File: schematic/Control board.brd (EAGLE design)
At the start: 41.6 x 67.3 mm, 14 parts, among them IC2 ATTINY44A

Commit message: Updated schematic, board file, and library; also updated the 3D model
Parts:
- moved POW1 3.86 mm to (24.1, 57.1)
- moved C1 3.86 mm to (19.1, 17.1), turned to 0 degrees
- moved REG1 3.86 mm to (20.3, 20.3)
- moved C2 3.24 mm to (26.7, 20.3), turned to 270 degrees
- renumbered ROTARY to ROTARY_P0915N, SLIDE to SLIDE_PTA2043
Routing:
- net +12V: track 89.6 -> 82.3 mm
- net +5V: track 100.6 -> 105.4 mm
- net GND: track 20.7 -> 16.1 mm
- net N$4: track 14.3 -> 13.4 mm

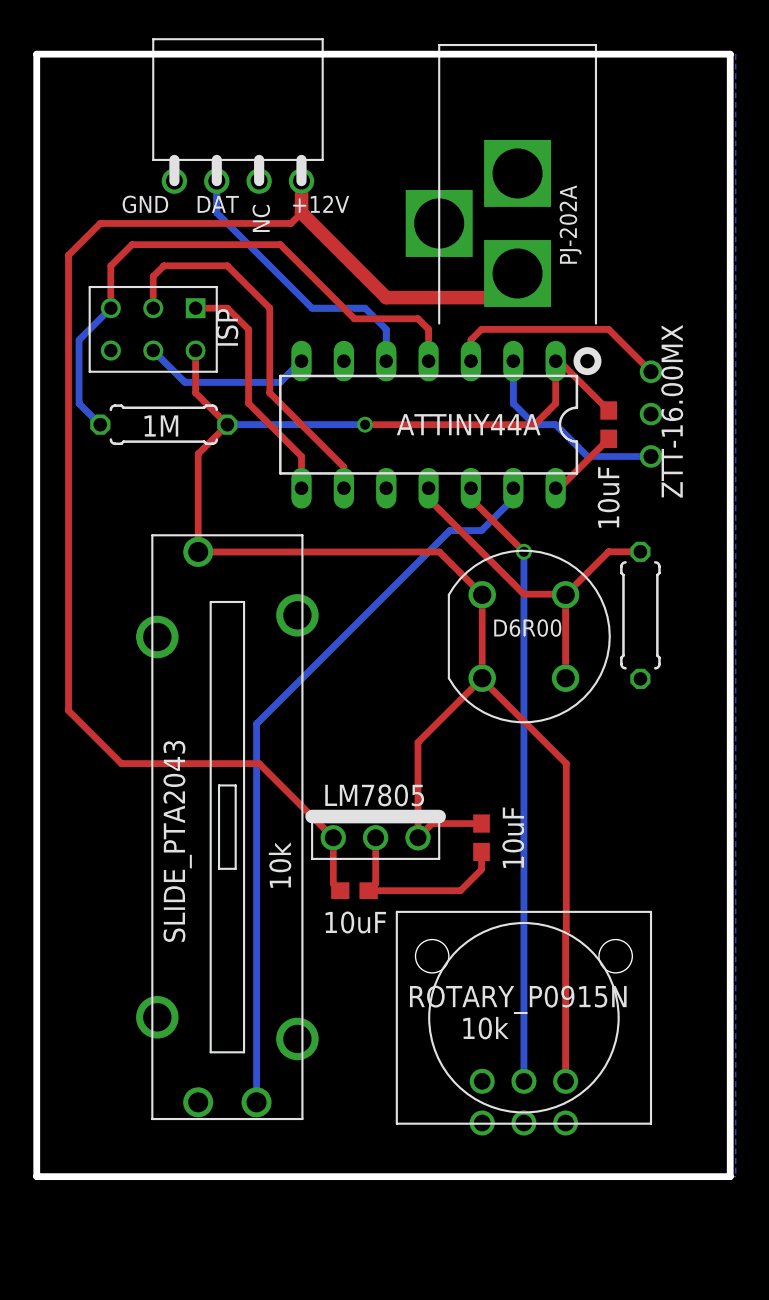
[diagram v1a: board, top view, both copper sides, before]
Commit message: Voltage regulator and DIP microcontroller are too big, replacing with small SMD components
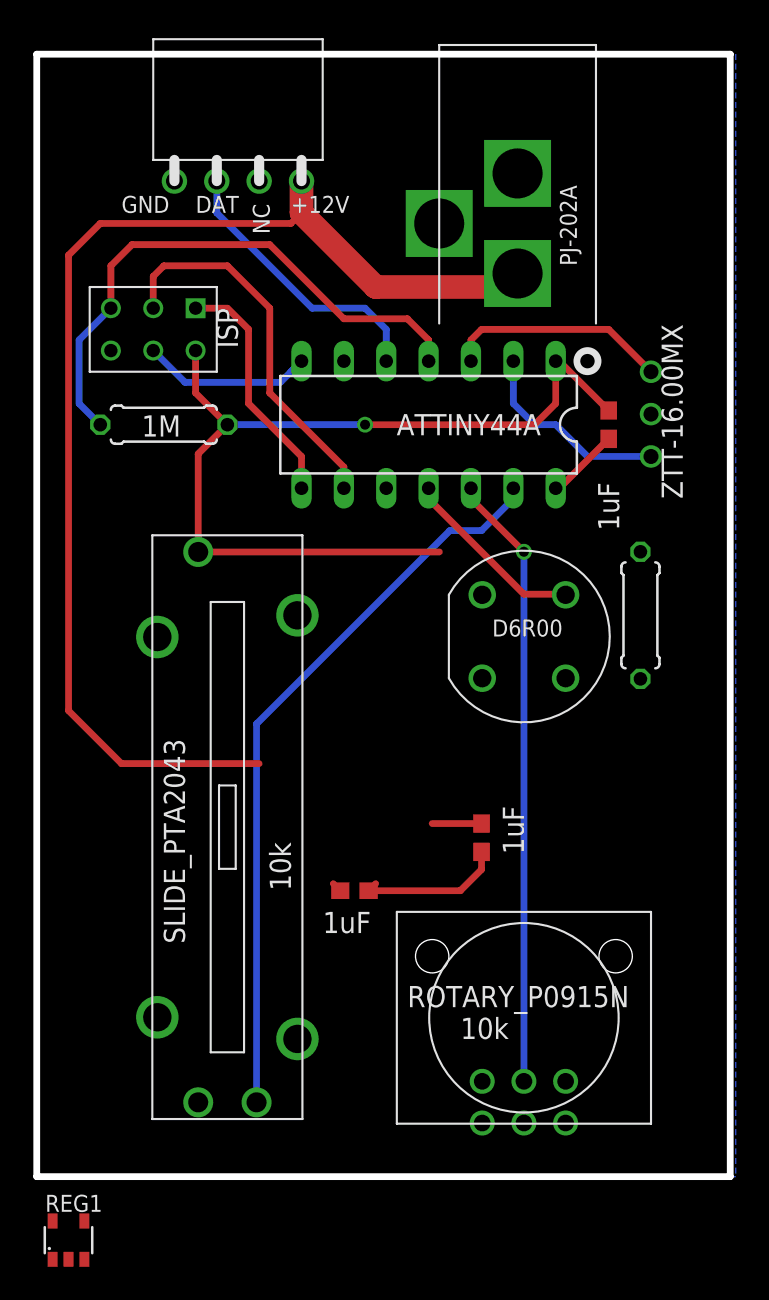
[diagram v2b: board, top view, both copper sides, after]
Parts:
- C1, C2, C3: value 10uF -> 1uF
- REG1: value LM7805 -> MIC5205; device RGB LED project:VREG_THROUGHHOLE -> RGB LED project:SOT-23-5
- moved REG1 30.4 mm to (1.91, -3.81)
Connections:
- net +12V: now also REG1.3
- net +5V: now also REG1.5; no longer REG1.3
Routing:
- net +5V: track 105.4 -> 58.2 mm
- net COLOR_SW: track 21.8 -> 11.2 mm
- net +12V: track 82.3 -> 72.7 mm
- net GND: track 16.1 -> 13.3 mm
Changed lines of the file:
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@@
 </autorouter>
 <elements>
-<element name="C1" library="resistor" package="C0603" value="10uF" x="19.05" y="17.145" smashed="yes">
+<element name="C1" library="resistor" package="C0603" value="1uF" x="19.05" y="17.145" smashed="yes">
 <attribute name="VALUE" x="17.145" y="14.605" size="1.27" layer="21" font="vector"/>
 </element>
@@
 </element>
 <element name="U$1" library="RGB LED project" package="ISP" value="ISP" x="6.985" y="50.8" smashed="yes" rot="R270"/>
-<element name="REG1" library="RGB LED project" package="VREG_THROUGHHOLE" value="LM7805" x="20.32" y="20.32" smashed="yes">
-<attribute name="VALUE" x="17.145" y="22.225" size="1.27" layer="21" font="vector"/>
-</element>
-<element name="C2" library="resistor" package="C0603" value="10uF" x="26.67" y="20.32" smashed="yes" rot="R270">
+<element name="C2" library="resistor" package="C0603" value="1uF" x="26.67" y="20.32" smashed="yes" rot="R270">
 <attribute name="VALUE" x="27.94" y="22.225" size="1.27" layer="21" font="vector" rot="R270"/>
 </element>
-<element name="C3" library="resistor" package="C0603" value="10uF" x="34.29" y="45.085" smashed="yes" rot="R270">
+<element name="C3" library="resistor" package="C0603" value="1uF" x="34.29" y="45.085" smashed="yes" rot="R270">
 <attribute name="VALUE" x="34.925" y="38.735" size="1.27" layer="21" font="vector" rot="R90"/>
 </element>
+<element name="REG1" library="RGB LED project" package="SOT-23-5" value="MIC5205" x="1.905" y="-3.81"/>
 </elements>
 <signals>
 <signal name="+5V">
 <contactref element="SLIDE_PTA2043" pad="P3"/>
-<contactref element="ROTARY_P0915N" pad="R13"/>
-<contactref element="S1" pad="1A"/>
-<contactref element="S1" pad="2A"/>
 <contactref element="IC2" pad="1"/>
 <contactref element="U$1" pad="VCC"/>
 <contactref element="R3" pad="1"/>
-<wire x1="26.71" y1="34.885" x2="26.71" y2="29.885" width="0.4064" layer="1"/>
-<contactref element="REG1" pad="3"/>
 <contactref element="C2" pad="1"/>
 <contactref element="C3" pad="1"/>
@@
 <wire x1="9.68" y1="43.335" x2="11.43" y2="45.085" width="0.4064" layer="1"/>
 <wire x1="9.68" y1="37.455" x2="24.14" y2="37.455" width="0.4064" layer="1"/>
-<wire x1="24.14" y1="37.455" x2="26.71" y2="34.885" width="0.4064" layer="1"/>
-<wire x1="31.71" y1="5.715" x2="31.71" y2="14.645" width="0.4064" layer="1"/>
-<wire x1="26.71" y1="29.885" x2="26.71" y2="29.805" width="0.4064" layer="1"/>
-<wire x1="26.71" y1="29.805" x2="31.75" y2="24.765" width="0.4064" layer="1"/>
-<wire x1="31.75" y1="24.765" x2="31.75" y2="14.685" width="0.4064" layer="1"/>
-<wire x1="31.75" y1="14.685" x2="31.71" y2="14.645" width="0.4064" layer="1"/>
 <wire x1="31.115" y1="48.895" x2="31.115" y2="46.355" width="0.4064" layer="1"/>
 <wire x1="31.115" y1="46.355" x2="29.845" y2="45.085" width="0.4064" layer="1"/>
@@
 <via x="19.685" y="45.085" extent="1-16" drill="0.6"/>
 <wire x1="19.685" y1="45.085" x2="11.43" y2="45.085" width="0.4064" layer="16"/>
-<wire x1="22.86" y1="20.32" x2="22.86" y2="26.035" width="0.4064" layer="1"/>
-<wire x1="22.86" y1="26.035" x2="26.71" y2="29.885" width="0.4064" layer="1"/>
 <wire x1="26.67" y1="21.17" x2="23.71" y2="21.17" width="0.4064" layer="1"/>
-<wire x1="23.71" y1="21.17" x2="22.86" y2="20.32" width="0.4064" layer="1"/>
+<contactref element="REG1" pad="5"/>
+<contactref element="S1" pad="1A"/>
+<contactref element="S1" pad="2A"/>
+<contactref element="ROTARY_P0915N" pad="R13"/>
+<wire x1="24.14" y1="37.455" x2="26.71" y2="34.885" width="0" layer="19" extent="1-1"/>
+<wire x1="26.71" y1="29.885" x2="26.71" y2="34.885" width="0" layer="19" extent="1-1"/>
+<wire x1="26.67" y1="21.17" x2="26.71" y2="29.885" width="0" layer="19" extent="1-1"/>
+<wire x1="31.71" y1="5.715" x2="26.67" y2="21.17" width="0" layer="19" extent="1-1"/>
+<wire x1="0.955" y1="-2.66" x2="31.71" y2="5.715" width="0" layer="19" extent="1-1"/>
 </signal>
 <signal name="SLIDE_V">
@@
 </signal>
 <signal name="COLOR_SW">
+<contactref element="IC2" pad="11"/>
+<wire x1="23.495" y1="41.275" x2="23.495" y2="40.64" width="0.4064" layer="1"/>
+<wire x1="23.495" y1="40.64" x2="29.21" y2="34.925" width="0.4064" layer="1"/>
+<wire x1="29.21" y1="34.925" x2="31.67" y2="34.925" width="0.4064" layer="1"/>
 <contactref element="S1" pad="1B"/>
 <contactref element="S1" pad="2B"/>
 <contactref element="R1" pad="2"/>
-<contactref element="IC2" pad="11"/>
-<wire x1="31.71" y1="34.885" x2="31.71" y2="29.885" width="0.4064" layer="1"/>
-<wire x1="36.195" y1="37.465" x2="34.29" y2="37.465" width="0.4064" layer="1"/>
-<wire x1="34.29" y1="37.465" x2="31.71" y2="34.885" width="0.4064" layer="1"/>
-<wire x1="23.495" y1="41.275" x2="23.495" y2="40.64" width="0.4064" layer="1"/>
-<wire x1="23.495" y1="40.64" x2="29.21" y2="34.925" width="0.4064" layer="1"/>
-<wire x1="29.21" y1="34.925" x2="31.67" y2="34.925" width="0.4064" layer="1"/>
-<wire x1="31.67" y1="34.925" x2="31.71" y2="34.885" width="0.4064" layer="1"/>
+<wire x1="31.71" y1="34.885" x2="36.195" y2="37.465" width="0" layer="19" extent="1-1"/>
+<wire x1="31.67" y1="34.925" x2="31.71" y2="34.885" width="0" layer="19" extent="1-1"/>
+<wire x1="31.71" y1="29.885" x2="31.71" y2="34.885" width="0" layer="19" extent="1-1"/>
 </signal>
 <signal name="GND">
@@
 <vertex x="0" y="0"/>
 </polygon>
-<contactref element="REG1" pad="2"/>
 <contactref element="C2" pad="2"/>
 <contactref element="C3" pad="2"/>
 <wire x1="31.115" y1="41.275" x2="31.33" y2="41.275" width="0.4064" layer="1"/>
 <wire x1="31.33" y1="41.275" x2="34.29" y2="44.235" width="0.4064" layer="1"/>
-<wire x1="20.32" y1="20.32" x2="20.32" y2="17.565" width="0.4064" layer="1"/>
 <wire x1="20.32" y1="17.565" x2="19.9" y2="17.145" width="0.4064" layer="1"/>
 <wire x1="26.67" y1="19.47" x2="26.67" y2="18.415" width="0.4064" layer="1"/>
 <wire x1="26.67" y1="18.415" x2="25.4" y2="17.145" width="0.4064" layer="1"/>
 <wire x1="25.4" y1="17.145" x2="19.9" y2="17.145" width="0.4064" layer="1"/>
+<contactref element="REG1" pad="2"/>
+<wire x1="26.71" y1="5.715" x2="25.4" y2="17.145" width="0" layer="19" extent="1-1"/>
+<wire x1="1.905" y1="-4.96" x2="9.68" y2="4.455" width="0" layer="19" extent="1-1"/>
 </signal>
 <signal name="+12V">
@@
 <contactref element="POW1" pad="1"/>
 <contactref element="CONN1" pad="P$4"/>
-<contactref element="REG1" pad="1"/>
-<wire x1="20.955" y1="52.705" x2="15.875" y2="57.785" width="0.8128" layer="1"/>
-<wire x1="15.875" y1="57.785" x2="15.875" y2="59.69" width="0.8128" layer="1"/>
+<wire x1="20.32" y1="53.34" x2="15.875" y2="57.785" width="1.4224" layer="1"/>
+<wire x1="15.875" y1="57.785" x2="15.875" y2="59.69" width="1.4224" layer="1"/>
 <wire x1="15.875" y1="57.785" x2="15.24" y2="57.15" width="0.4064" layer="1"/>
 <wire x1="15.24" y1="57.15" x2="3.81" y2="57.15" width="0.4064" layer="1"/>
@@
 <wire x1="1.905" y1="55.245" x2="1.905" y2="27.94" width="0.4064" layer="1"/>
 <wire x1="1.905" y1="27.94" x2="5.08" y2="24.765" width="0.4064" layer="1"/>
-<wire x1="20.955" y1="52.705" x2="27.385" y2="52.705" width="0.8128" layer="1"/>
-<wire x1="27.385" y1="52.705" x2="28.83" y2="54.15" width="0.8128" layer="1"/>
+<wire x1="20.32" y1="53.34" x2="28.02" y2="53.34" width="1.4224" layer="1"/>
+<wire x1="28.02" y1="53.34" x2="28.83" y2="54.15" width="1.4224" layer="1"/>
 <wire x1="5.08" y1="24.765" x2="13.335" y2="24.765" width="0.4064" layer="1"/>
-<wire x1="13.335" y1="24.765" x2="17.78" y2="20.32" width="0.4064" layer="1"/>
-<wire x1="17.78" y1="20.32" x2="17.78" y2="17.565" width="0.4064" layer="1"/>
 <wire x1="17.78" y1="17.565" x2="18.2" y2="17.145" width="0.4064" layer="1"/>
+<contactref element="REG1" pad="1"/>
+<contactref element="REG1" pad="3"/>
+<wire x1="13.335" y1="24.765" x2="17.78" y2="17.565" width="0" layer="19" extent="1-1"/>
+<wire x1="2.855" y1="-4.96" x2="18.2" y2="17.145" width="0" layer="19" extent="1-1"/>
+<wire x1="0.955" y1="-4.96" x2="2.855" y2="-4.96" width="0" layer="19" extent="1-1"/>
 </signal>
 <signal name="N$2">
@@
 <wire x1="2.54" y1="50.165" x2="2.54" y2="46.355" width="0.4064" layer="16"/>
 <wire x1="2.54" y1="46.355" x2="3.81" y2="45.085" width="0.4064" layer="16"/>
-<wire x1="23.495" y1="48.895" x2="23.495" y2="50.8" width="0.4064" layer="1"/>
-<wire x1="23.495" y1="50.8" x2="22.86" y2="51.435" width="0.4064" layer="1"/>
-<wire x1="22.86" y1="51.435" x2="19.05" y2="51.435" width="0.4064" layer="1"/>
-<wire x1="19.05" y1="51.435" x2="14.605" y2="55.88" width="0.4064" layer="1"/>
-<wire x1="14.605" y1="55.88" x2="5.715" y2="55.88" width="0.4064" layer="1"/>
+<wire x1="23.495" y1="48.895" x2="23.495" y2="50.165" width="0.4064" layer="1"/>
+<wire x1="23.495" y1="50.165" x2="22.225" y2="51.435" width="0.4064" layer="1"/>
+<wire x1="22.225" y1="51.435" x2="18.415" y2="51.435" width="0.4064" layer="1"/>
+<wire x1="18.415" y1="51.435" x2="13.97" y2="55.88" width="0.4064" layer="1"/>
+<wire x1="13.97" y1="55.88" x2="5.715" y2="55.88" width="0.4064" layer="1"/>
 <wire x1="5.715" y1="55.88" x2="4.445" y2="54.61" width="0.4064" layer="1"/>
 <wire x1="4.445" y1="54.61" x2="4.445" y2="52.07" width="0.4064" layer="1"/>

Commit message: Updated board with QFN-20 microcontroller
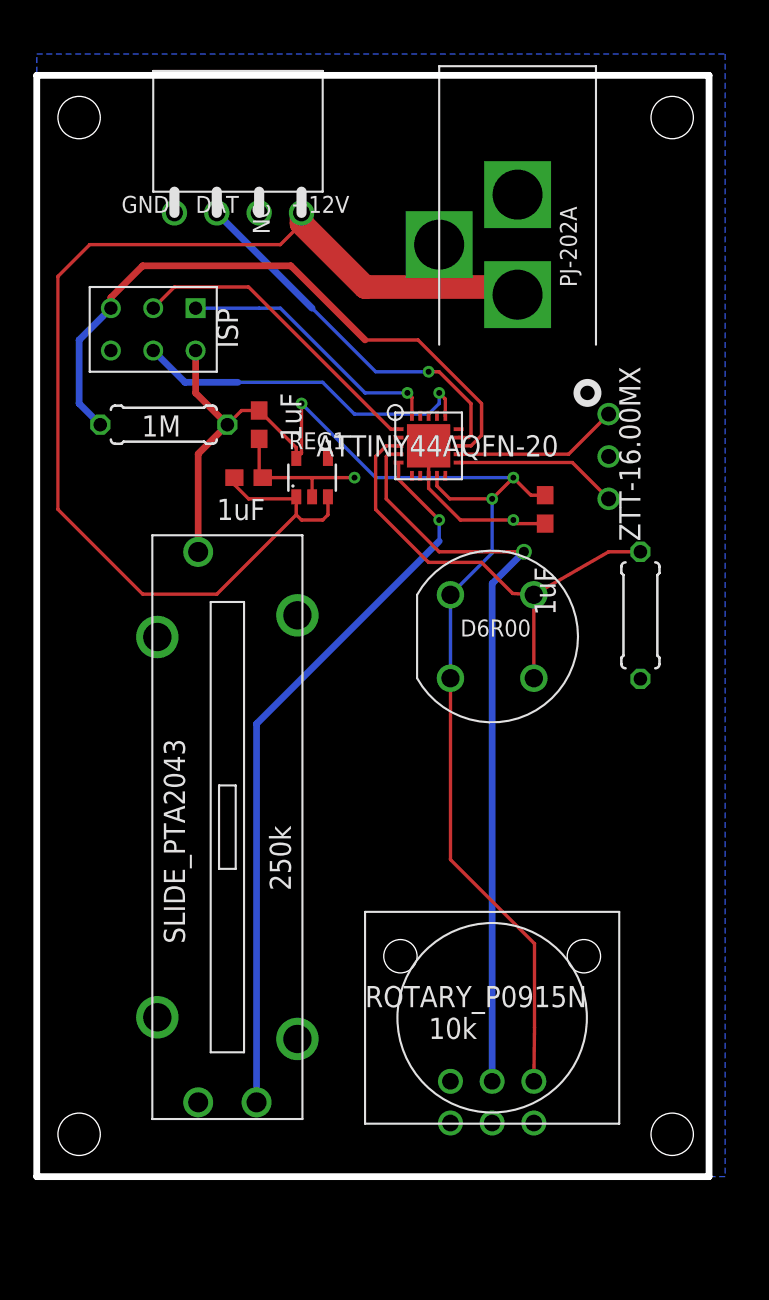
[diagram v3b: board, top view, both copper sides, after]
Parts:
- IC2: value ATTINY44A -> ATTINY44AQFN-20; device RGB LED project:PDIP-14 -> RGB LED project:QFN-20
- SLIDE_PTA2043: value 10k -> 250k
- moved REG1 48.0 mm to (16.5, 41.9)
- moved C2 28.1 mm to (13.3, 45.1)
- moved C1 25.6 mm to (12.7, 41.9)
- moved C3 6.35 mm to (30.5, 40.0)
- moved RES1 3.59 mm to (34.3, 43.2)
- moved CONN1 1.91 mm to (12.1, 57.8)
- moved ROTARY_P0915N 1.91 mm to (27.3, 5.71)
- moved S1 1.91 mm to (27.3, 32.4)
- moved IC2 1.27 mm to (23.5, 43.8), turned to 0 degrees
- moved POW1 1.27 mm to (24.1, 55.9)
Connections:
- net +5V: now also IC2.P$9; no longer IC2.1
- net COLOR_SW: now also IC2.P$3; no longer IC2.11
- net GND: now also IC2.P$8, IC2.PAD; no longer IC2.14
- net LED_SIGNAL: now also IC2.P$14; no longer IC2.5
- net MISO: now also IC2.P$20; no longer IC2.8
- net MOSI: now also IC2.P$16; no longer IC2.7
- net N$2: now also IC2.P$11; no longer IC2.2
- net N$4: now also IC2.P$12; no longer IC2.3
- net RESET: now also IC2.P$13; no longer IC2.4
- net ROT_V: now also IC2.P$4; no longer IC2.12
- net SCK: now also IC2.P$1; no longer IC2.9
- net SLIDE_V: now also IC2.P$5; no longer IC2.13
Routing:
- net +5V: track 58.2 -> 84.0 mm, vias 1 -> 3
- net COLOR_SW: track 11.2 -> 28.5 mm
- net MOSI: track 11.1 -> 21.1 mm, vias 0 -> 1
- net ROT_V: track 36.9 -> 45.4 mm
- net GND: track 13.3 -> 19.7 mm, vias 0 -> 2
- net LED_SIGNAL: track 16.9 -> 22.7 mm, vias 0 -> 1
- net RESET: track 34.1 -> 38.9 mm
- net SCK: track 22.8 -> 18.8 mm
- net N$4: track 13.4 -> 9.99 mm
- net N$2: track 12.1 -> 9.90 mm
- net MISO: track 14.5 -> 16.3 mm, vias 0 -> 1
- net SLIDE_V: track 44.3 -> 43.9 mm, vias 0 -> 1
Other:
- board size 41.6 x 67.3 mm -> 40.3 x 66 mm
